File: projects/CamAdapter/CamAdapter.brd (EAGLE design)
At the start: 22.5 x 41.9 mm, 3 parts

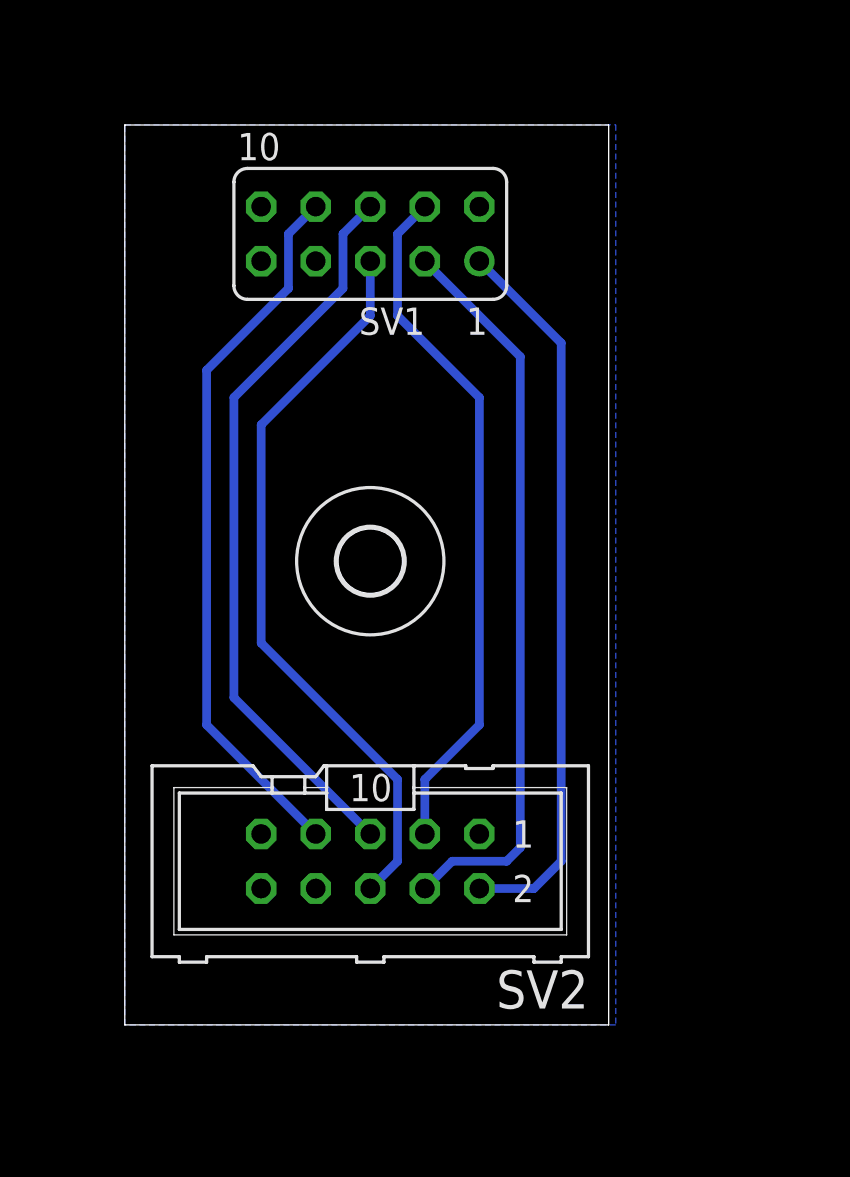
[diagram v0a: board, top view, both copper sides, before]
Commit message: Updated CamAdapter + Board
* Added 25 MHz resonator to adapter board
* Removed 25 MHz CLK signal from PCB connector
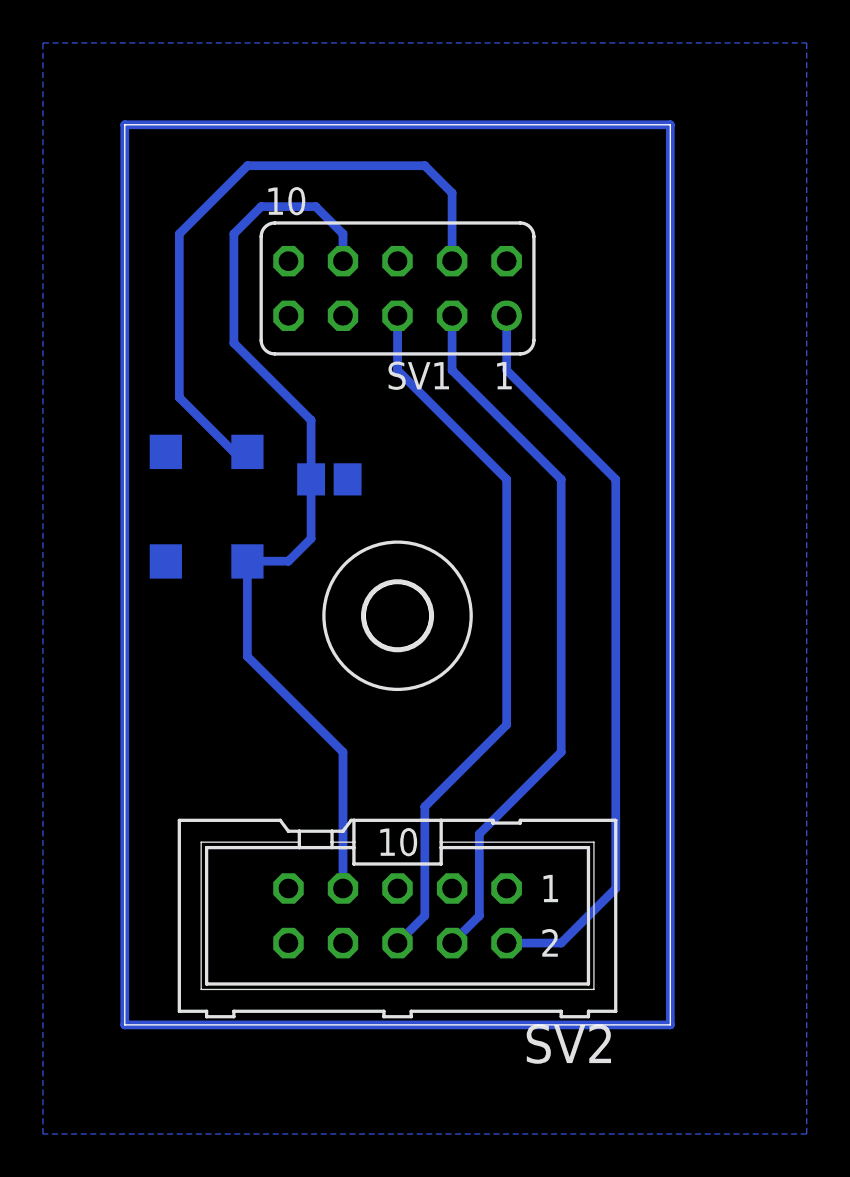
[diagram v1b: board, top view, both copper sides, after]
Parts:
- added C1: (no value), resistor:C0805
- added QG1: SM77H, crystal:SM77H
- moved SV2 2.84 mm to (12.7, 5.08)
- moved SV1 2.84 mm to (12.7, 34.3)
- moved U$1 2.84 mm to (12.7, 19.1)
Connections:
- new net N$1: QG1.3, SV1.4
- net CLK: no longer SV1.4
- net GND: now also C1.2, QG1.2
- net VCC: now also C1.1, QG1.4
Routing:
- net N$2: track 0.00 -> 134.6 mm
- net SCL: track 34.5 -> 0.00 mm
- net CLK: track 32.4 -> 0.00 mm
- net N$1: track 0.00 -> 29.6 mm
- net VCC: track 33.4 -> 43.6 mm
- net RESET#: track 33.9 -> 34.9 mm
- net CE#: track 34.5 -> 33.4 mm
- net SDA: track 34.4 -> 33.4 mm
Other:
- board size 22.5 x 41.9 mm -> 25.4 x 41.9 mm

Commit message: Rev 2.0 RC
* TODO: Check CamAdapter.brd quarz oscillator package
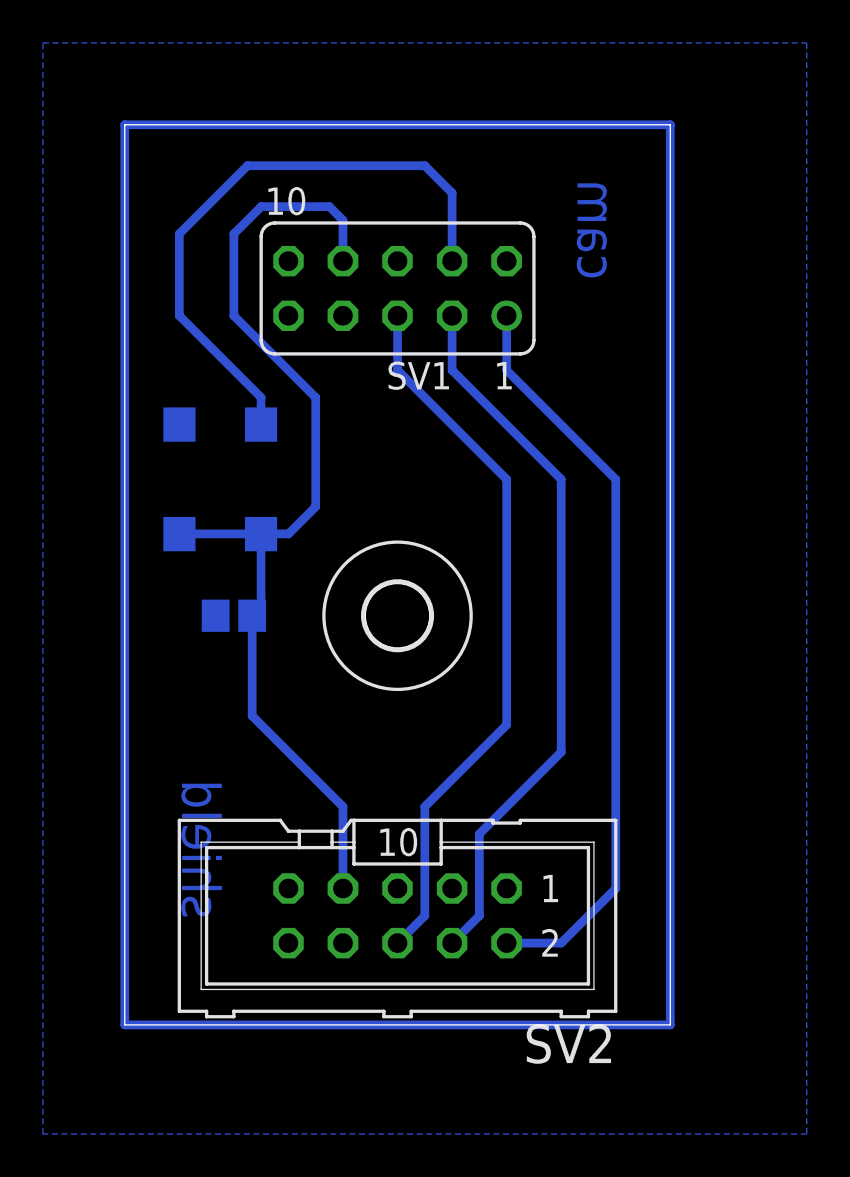
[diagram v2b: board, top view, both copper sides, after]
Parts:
- C1: value (none) -> 100n
- moved C1 7.75 mm to (5.08, 19.1), turned to 0 degrees
- moved QG1 1.42 mm to (4.45, 25.4)
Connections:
- net VCC: now also QG1.1
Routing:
- net VCC: track 43.6 -> 47.4 mm
- net N$1: track 29.6 -> 28.2 mm
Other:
- board text added: "cam"
- board text added: "shield"
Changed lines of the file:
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@@
 <wire x1="25.4" y1="41.91" x2="0" y2="41.91" width="0" layer="20"/>
 <wire x1="0" y1="41.91" x2="0" y2="0" width="0" layer="20"/>
+<text x="22.86" y="39.37" size="1.778" layer="16" font="vector" ratio="15" rot="MR270">cam</text>
+<text x="4.445" y="11.43" size="1.778" layer="16" font="vector" ratio="15" rot="MR270">shield</text>
 </plain>
 <attributes>
@@
 </element>
 <element name="U$1" library="holes" package="3,0" value="" x="12.7" y="19.05"/>
-<element name="QG1" library="crystal" package="SM77H" value="SM77H" x="3.81" y="24.13" rot="MR90">
-<attribute name="OC_NEWARK" value="unknown" x="3.81" y="24.13" size="1.778" layer="28" rot="MR90" display="off"/>
-<attribute name="MPN" value="" x="3.81" y="24.13" size="1.778" layer="28" rot="MR90" display="off"/>
-<attribute name="MF" value="" x="3.81" y="24.13" size="1.778" layer="28" rot="MR90" display="off"/>
-<attribute name="OC_FARNELL" value="unknown" x="3.81" y="24.13" size="1.778" layer="28" rot="MR90" display="off"/>
+<element name="QG1" library="crystal" package="SM77H" value="SM77H" x="4.445" y="25.4" rot="MR90">
+<attribute name="OC_NEWARK" value="unknown" x="4.445" y="25.4" size="1.778" layer="28" rot="MR90" display="off"/>
+<attribute name="MPN" value="" x="4.445" y="25.4" size="1.778" layer="28" rot="MR90" display="off"/>
+<attribute name="MF" value="" x="4.445" y="25.4" size="1.778" layer="28" rot="MR90" display="off"/>
+<attribute name="OC_FARNELL" value="unknown" x="4.445" y="25.4" size="1.778" layer="28" rot="MR90" display="off"/>
 </element>
-<element name="C1" library="resistor" package="C0805" value="" x="9.525" y="25.4" rot="MR180"/>
+<element name="C1" library="resistor" package="C0805" value="100n" x="5.08" y="19.05" rot="MR0"/>
 </elements>
 <signals>
@@
 <contactref element="QG1" pad="4"/>
 <contactref element="C1" pad="1"/>
-<wire x1="10.16" y1="6.35" x2="10.16" y2="12.7" width="0.4064" layer="16"/>
+<wire x1="6.355" y1="22.86" x2="6.345" y2="22.85" width="0.4064" layer="16"/>
+<wire x1="5.93" y1="19.05" x2="5.93" y2="14.39" width="0.4064" layer="16"/>
+<wire x1="5.93" y1="14.39" x2="10.16" y2="10.16" width="0.4064" layer="16"/>
+<wire x1="10.16" y1="10.16" x2="10.16" y2="6.35" width="0.4064" layer="16"/>
+<wire x1="6.345" y1="22.85" x2="6.345" y2="19.465" width="0.4064" layer="16"/>
+<wire x1="6.345" y1="19.465" x2="5.93" y2="19.05" width="0.4064" layer="16"/>
+<wire x1="6.355" y1="22.86" x2="7.62" y2="22.86" width="0.4064" layer="16"/>
+<wire x1="7.62" y1="22.86" x2="8.89" y2="24.13" width="0.4064" layer="16"/>
+<wire x1="8.89" y1="24.13" x2="8.89" y2="29.21" width="0.4064" layer="16"/>
+<wire x1="8.89" y1="29.21" x2="5.08" y2="33.02" width="0.4064" layer="16"/>
+<wire x1="5.08" y1="33.02" x2="5.08" y2="36.83" width="0.4064" layer="16"/>
 <wire x1="5.08" y1="36.83" x2="6.35" y2="38.1" width="0.4064" layer="16"/>
-<wire x1="6.35" y1="38.1" x2="8.89" y2="38.1" width="0.4064" layer="16"/>
-<wire x1="8.89" y1="38.1" x2="10.16" y2="36.83" width="0.4064" layer="16"/>
-<wire x1="10.16" y1="36.83" x2="10.16" y2="35.56" width="0.4064" layer="16"/>
-<wire x1="5.08" y1="31.75" x2="5.08" y2="36.83" width="0.4064" layer="16"/>
-<wire x1="5.71" y1="21.58" x2="5.71" y2="17.15" width="0.4064" layer="16"/>
-<wire x1="5.71" y1="17.15" x2="10.16" y2="12.7" width="0.4064" layer="16"/>
-<wire x1="8.675" y1="25.4" x2="8.675" y2="22.645" width="0.4064" layer="16"/>
-<wire x1="8.675" y1="22.645" x2="7.62" y2="21.59" width="0.4064" layer="16"/>
-<wire x1="7.62" y1="21.59" x2="5.72" y2="21.59" width="0.4064" layer="16"/>
-<wire x1="5.72" y1="21.59" x2="5.71" y2="21.58" width="0.4064" layer="16"/>
-<wire x1="8.675" y1="25.4" x2="8.675" y2="28.155" width="0.4064" layer="16"/>
-<wire x1="8.675" y1="28.155" x2="5.08" y2="31.75" width="0.4064" layer="16"/>
+<wire x1="6.35" y1="38.1" x2="9.525" y2="38.1" width="0.4064" layer="16"/>
+<wire x1="9.525" y1="38.1" x2="10.16" y2="37.465" width="0.4064" layer="16"/>
+<wire x1="10.16" y1="37.465" x2="10.16" y2="35.56" width="0.4064" layer="16"/>
+<contactref element="QG1" pad="1"/>
+<wire x1="6.355" y1="22.86" x2="2.555" y2="22.86" width="0.4064" layer="16"/>
+<wire x1="2.555" y1="22.86" x2="2.545" y2="22.85" width="0.4064" layer="16"/>
 </signal>
 <signal name="N$1">
@@
 <wire x1="13.97" y1="40.005" x2="15.24" y2="38.735" width="0.4064" layer="16"/>
 <wire x1="15.24" y1="38.735" x2="15.24" y2="35.56" width="0.4064" layer="16"/>
-<wire x1="5.71" y1="26.68" x2="5.07" y2="26.68" width="0.4064" layer="16"/>
-<wire x1="5.07" y1="26.68" x2="2.54" y2="29.21" width="0.4064" layer="16"/>
-<wire x1="2.54" y1="29.21" x2="2.54" y2="36.83" width="0.4064" layer="16"/>
+<wire x1="6.345" y1="27.95" x2="6.345" y2="29.215" width="0.4064" layer="16"/>
+<wire x1="6.345" y1="29.215" x2="2.54" y2="33.02" width="0.4064" layer="16"/>
+<wire x1="2.54" y1="33.02" x2="2.54" y2="36.83" width="0.4064" layer="16"/>
 </signal>
 <signal name="N$2">

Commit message: Fixed forgotten SCL line
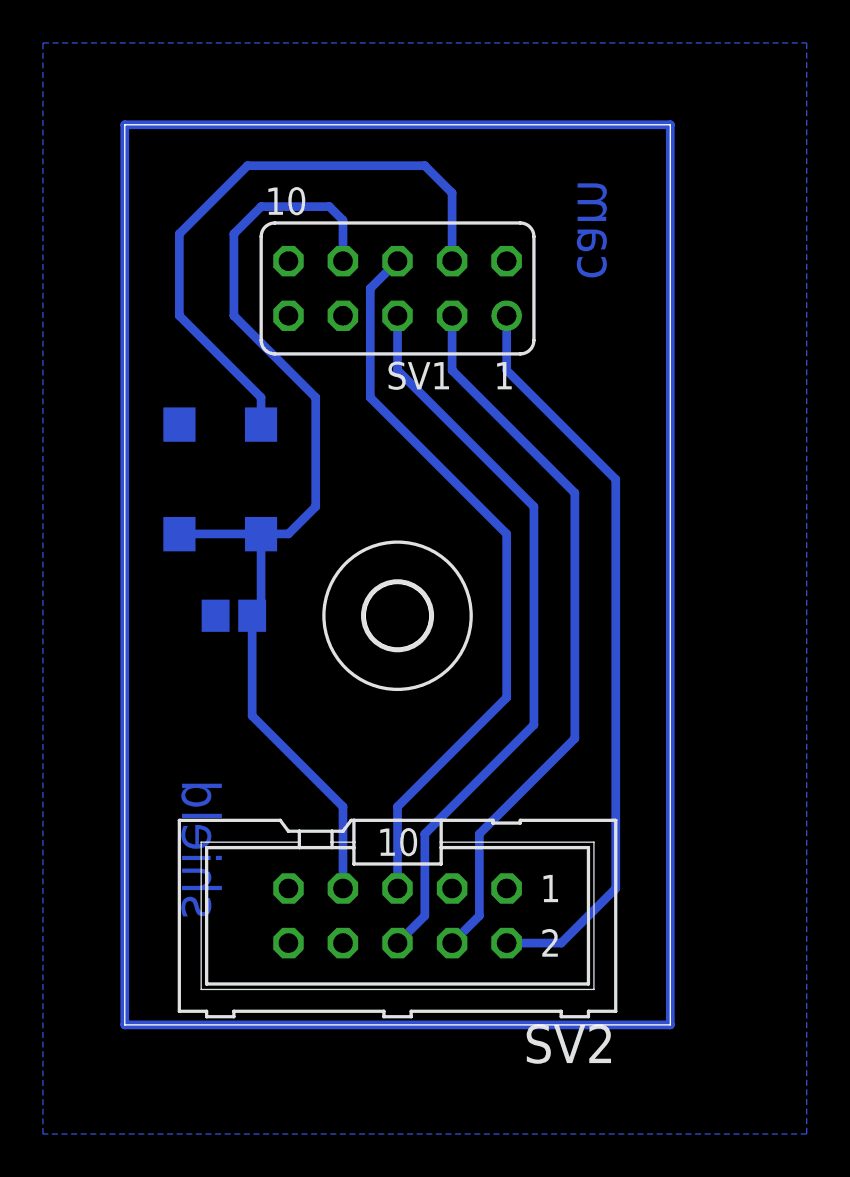
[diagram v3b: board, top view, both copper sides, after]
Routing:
- net SCL: track 0.00 -> 34.5 mm
- net CE#: track 33.4 -> 34.5 mm
- net SDA: track 33.4 -> 33.9 mm
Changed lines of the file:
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@@
 <wire x1="15.24" y1="3.81" x2="16.51" y2="5.08" width="0.4064" layer="16"/>
 <wire x1="16.51" y1="5.08" x2="16.51" y2="8.89" width="0.4064" layer="16"/>
-<wire x1="20.32" y1="25.4" x2="15.24" y2="30.48" width="0.4064" layer="16"/>
+<wire x1="20.955" y1="24.765" x2="15.24" y2="30.48" width="0.4064" layer="16"/>
 <wire x1="15.24" y1="30.48" x2="15.24" y2="33.02" width="0.4064" layer="16"/>
-<wire x1="16.51" y1="8.89" x2="20.32" y2="12.7" width="0.4064" layer="16"/>
-<wire x1="20.32" y1="12.7" x2="20.32" y2="25.4" width="0.4064" layer="16"/>
+<wire x1="16.51" y1="8.89" x2="20.955" y2="13.335" width="0.4064" layer="16"/>
+<wire x1="20.955" y1="13.335" x2="20.955" y2="24.765" width="0.4064" layer="16"/>
 </signal>
 <signal name="SCL">
 <contactref element="SV2" pad="5"/>
 <contactref element="SV1" pad="6"/>
-<wire x1="12.7" y1="6.35" x2="12.7" y2="35.56" width="0" layer="19" extent="1-1"/>
+<wire x1="12.7" y1="6.35" x2="12.7" y2="10.16" width="0.4064" layer="16"/>
+<wire x1="12.7" y1="10.16" x2="17.78" y2="15.24" width="0.4064" layer="16"/>
+<wire x1="17.78" y1="15.24" x2="17.78" y2="22.86" width="0.4064" layer="16"/>
+<wire x1="17.78" y1="22.86" x2="11.43" y2="29.21" width="0.4064" layer="16"/>
+<wire x1="11.43" y1="29.21" x2="11.43" y2="34.29" width="0.4064" layer="16"/>
+<wire x1="11.43" y1="34.29" x2="12.7" y2="35.56" width="0.4064" layer="16"/>
 </signal>
 <signal name="CE#">
@@
 <contactref element="SV1" pad="5"/>
 <wire x1="12.7" y1="3.81" x2="13.97" y2="5.08" width="0.4064" layer="16"/>
-<wire x1="13.97" y1="5.08" x2="13.97" y2="10.16" width="0.4064" layer="16"/>
-<wire x1="17.78" y1="13.97" x2="17.78" y2="25.4" width="0.4064" layer="16"/>
-<wire x1="17.78" y1="25.4" x2="12.7" y2="30.48" width="0.4064" layer="16"/>
+<wire x1="13.97" y1="5.08" x2="13.97" y2="8.89" width="0.4064" layer="16"/>
+<wire x1="19.05" y1="13.97" x2="19.05" y2="24.13" width="0.4064" layer="16"/>
+<wire x1="19.05" y1="24.13" x2="12.7" y2="30.48" width="0.4064" layer="16"/>
 <wire x1="12.7" y1="30.48" x2="12.7" y2="33.02" width="0.4064" layer="16"/>
-<wire x1="13.97" y1="10.16" x2="17.78" y2="13.97" width="0.4064" layer="16"/>
+<wire x1="13.97" y1="8.89" x2="19.05" y2="13.97" width="0.4064" layer="16"/>
 </signal>
 <signal name="GND">
